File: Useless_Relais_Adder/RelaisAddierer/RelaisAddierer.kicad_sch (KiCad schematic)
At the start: 254 parts, among them J1 Conn_01x08_Pin, J2 Barrel_Jack, K201 HK19F-DCxxV-SHC, K202 HK19F-DCxxV-SHC, K203 HK19F-DCxxV-SHC, K204 HK19F-DCxxV-SHC, K205 HK19F-DCxxV-SHC, K206 HK19F-DCxxV-SHC, K207 HK19F-DCxxV-SHC, K208 HK19F-DCxxV-SHC, K209 HK19F-DCxxV-SHC, K210 HK19F-DCxxV-SHC, K211 HK19F-DCxxV-SHC, K212 HK19F-DCxxV-SHC, K213 HK19F-DCxxV-SHC, K214 HK19F-DCxxV-SHC, K215 HK19F-DCxxV-SHC, K216 HK19F-DCxxV-SHC, K217 HK19F-DCxxV-SHC, K218 HK19F-DCxxV-SHC, K219 HK19F-DCxxV-SHC, K220 HK19F-DCxxV-SHC, K221 HK19F-DCxxV-SHC, K222 HK19F-DCxxV-SHC, K223 HK19F-DCxxV-SHC, K224 HK19F-DCxxV-SHC, K225 HK19F-DCxxV-SHC, K226 HK19F-DCxxV-SHC, K227 HK19F-DCxxV-SHC, K228 HK19F-DCxxV-SHC, K229 HK19F-DCxxV-SHC, K230 HK19F-DCxxV-SHC, K231 HK19F-DCxxV-SHC, K232 HK19F-DCxxV-SHC, Q1 BC847, Q10 BC847, Q11 DMP3099L, Q12 DMP3099L, Q13 DMP3099L, Q14 DMP3099L, Q15 DMP3099L, Q16 DMP3099L, Q17 BC847, Q18 BC847, Q19 BC847, Q2 BC847, Q20 BC847, Q201 BSS138, Q202 BSS138, Q21 BC847, Q22 DMP3099L, Q23 BC847, Q24 BC847, Q25 DMP3099L, Q26 BC847, Q27 DMP3099L, Q28 DMP3099L, Q29 DMP3099L, Q3 BC847, Q30 DMP3099L, Q31 DMP3099L, Q32 DMP3099L, Q4 BC847, Q5 BC847, Q6 PJM10H01PSA, Q7 BC847, Q8 BC847, Q9 DMP3099L, SW1 RotaryEncoder_Switch, SW2 RotaryEncoder_Switch, U1 TCA9534, U2 TCA9534, U3 TCA9534, U4 uA7805

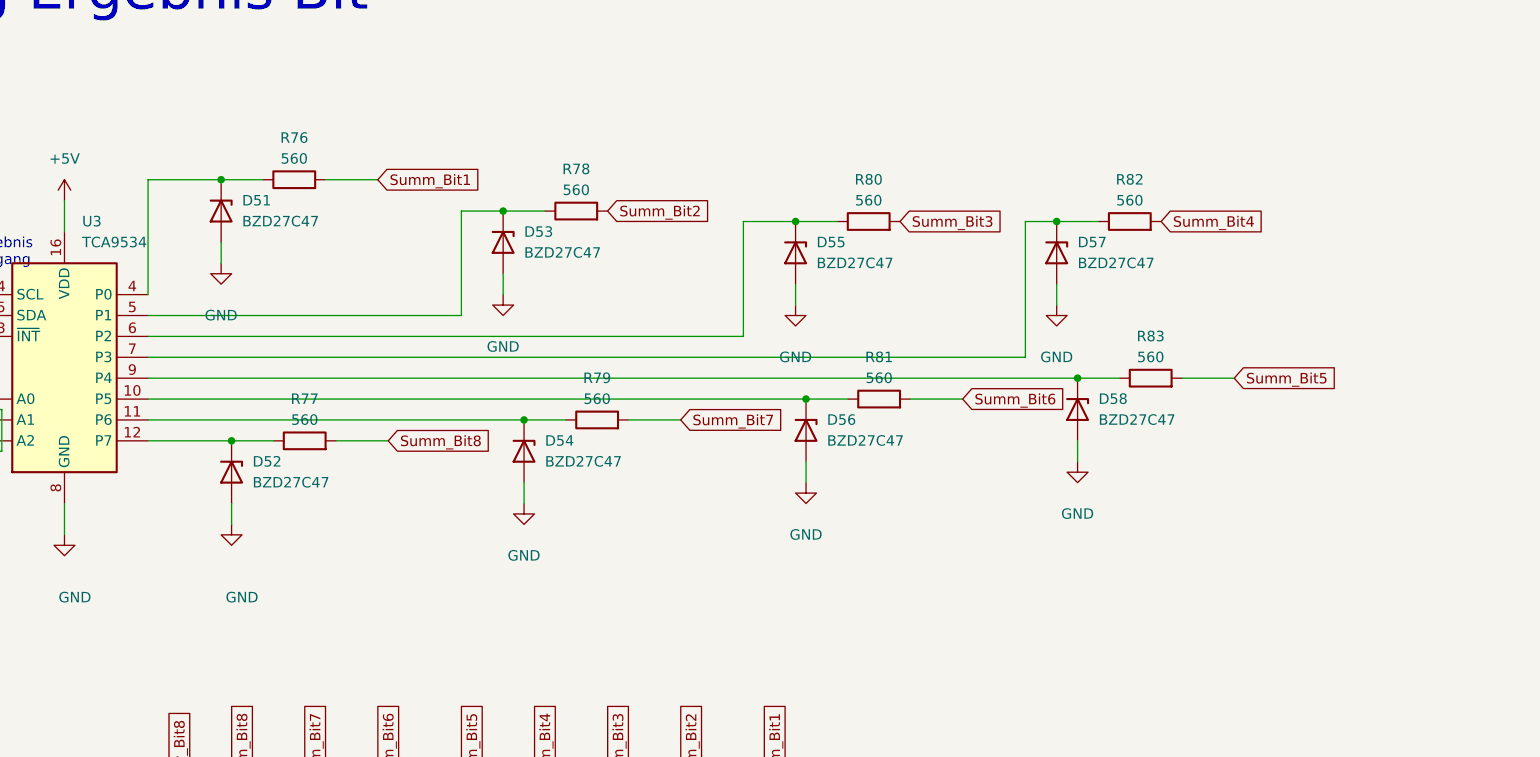
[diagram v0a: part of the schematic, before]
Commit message: Spannungsteiler statt Widerstand für Eingangsstufe
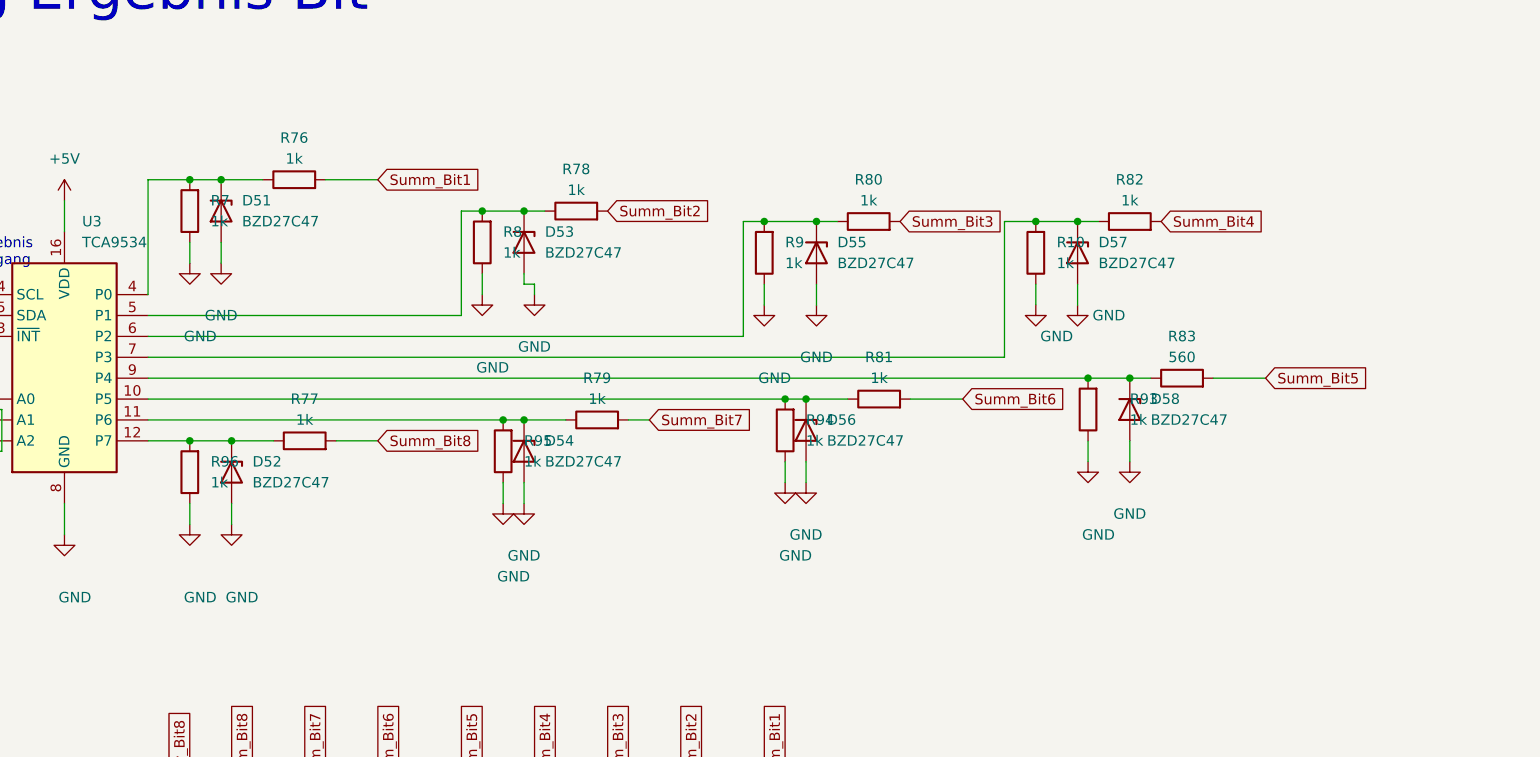
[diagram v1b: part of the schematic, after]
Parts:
- added R10, R7, R8, R9, R93, R94, R95, R96: 1k, Resistor_SMD:R_0805_2012Metric_Pad1.20x1.40mm_HandSolder, symbol Device:R
- R76, R77, R78, R79, R80, R81, R82: value 560 -> 1k
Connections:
- net GND: now also R10.1, R7.1, R8.1, R9.1, R93.1, R94.1, R95.1, R96.1
- net at D57.1 (K), R82.1, U3.7 (P3): now also R10.2
- net at D54.1 (K), R79.1, U3.11 (P6): now also R95.2
- net at D56.1 (K), R81.1, U3.10 (P5): now also R94.2
- net at D52.1 (K), R77.1, U3.12 (P7): now also R96.2
- net at D51.1 (K), R76.1, U3.4 (P0): now also R7.2
- net at D53.1 (K), R78.1, U3.5 (P1): now also R8.2
- net at D55.1 (K), R80.1, U3.6 (P2): now also R9.2
- net at D58.1 (K), R83.1, U3.9 (P4): now also R93.2
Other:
- moved on the sheet: D53, D55, D57, D58, R83
